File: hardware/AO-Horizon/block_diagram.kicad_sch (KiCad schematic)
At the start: 0 parts

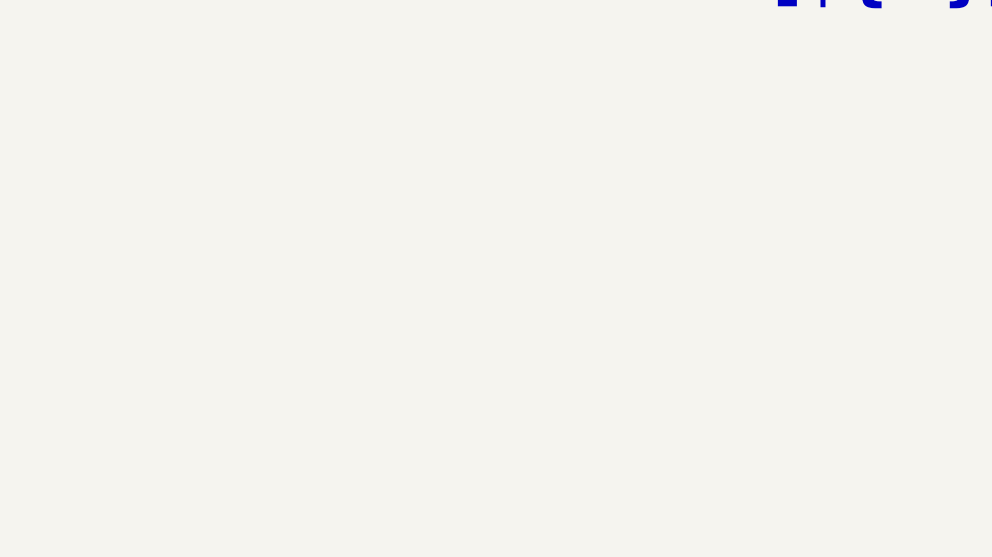
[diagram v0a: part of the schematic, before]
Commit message: feat(power): add TPS62142 3V3 buck and new library parts (#6)
* docs(readme): simplify workflow diagram explanation

Mark DRAFT as under review, sync CHECK label, and add a colour key in README and template.

Co-Authored-By: Claude Sonnet 5.5 <noreply@anthropic.com>

* Update settings.json

* change spec file name

* update git-workflow skill

* change skill name by add hw-*

* docs: update AeroOptix-Horizon hardware spec

* docs: consolidate hardware handoff into checklist

* Update CLAUDE.md

* Update CLAUDE.md

* Update CLAUDE.md

* feat(hooks): replace protect hook with rule-based v2

Move file-protection rules into hooks/protect.json (allow > deny > ask)
and use ask for editable-with-approval files instead of a hard block.
Bash/PowerShell checks now inspect write targets, not any mention of a
protected path. Align settings.json permissions and drop the old hook.

Co-Authored-By: Claude Sonnet 5.5 <noreply@anthropic.com>

* docs: update CLAUDE.md for protection tiers and skill names

Describe the ask/deny protection rules, the v2 hook and protect.json,
and fix stale skill and template names.

Co-Authored-By: Claude Sonnet 5.5 <noreply@anthropic.com>

* Update .gitignore

* Update .gitignore

* Update .gitignore

* del skills

* Update engineering.md

* Update git-workflow.md

* Update hardware-workflow.md

* Update settings.json

* Update pull_request_template.md

* Update .gitignore

* Update .gitignore

* Delete SKILL.md

* Delete SKILL.md

* Update .gitignore

* add git-workflow skill

* Update CLAUDE.md

* Update protect.json

* Update settings.json

* Create MEMORY.md

* feat(agents): add codex-hw-delegate for bounded Codex tasks

Add a project agent that delegates one small, read-only-by-default task
to Codex CLI. It gates trivial or ambiguous requests, refuses PDF and
KiCad file contents, never mutates git, cross-checks Codex output and
returns a fixed report format.

Co-Authored-By: Claude Sonnet 5.5 <noreply@anthropic.com>

* fix(hooks): resolve .. and 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
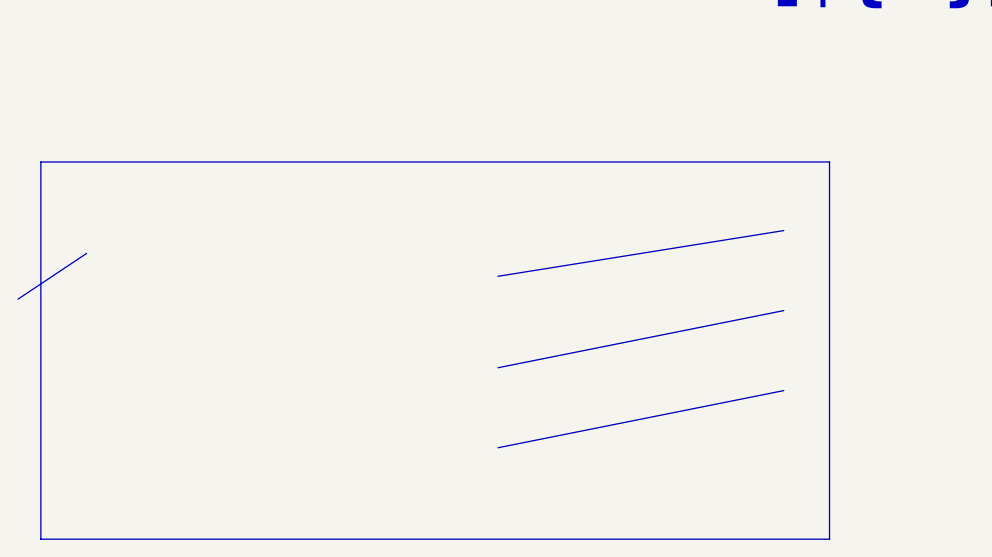
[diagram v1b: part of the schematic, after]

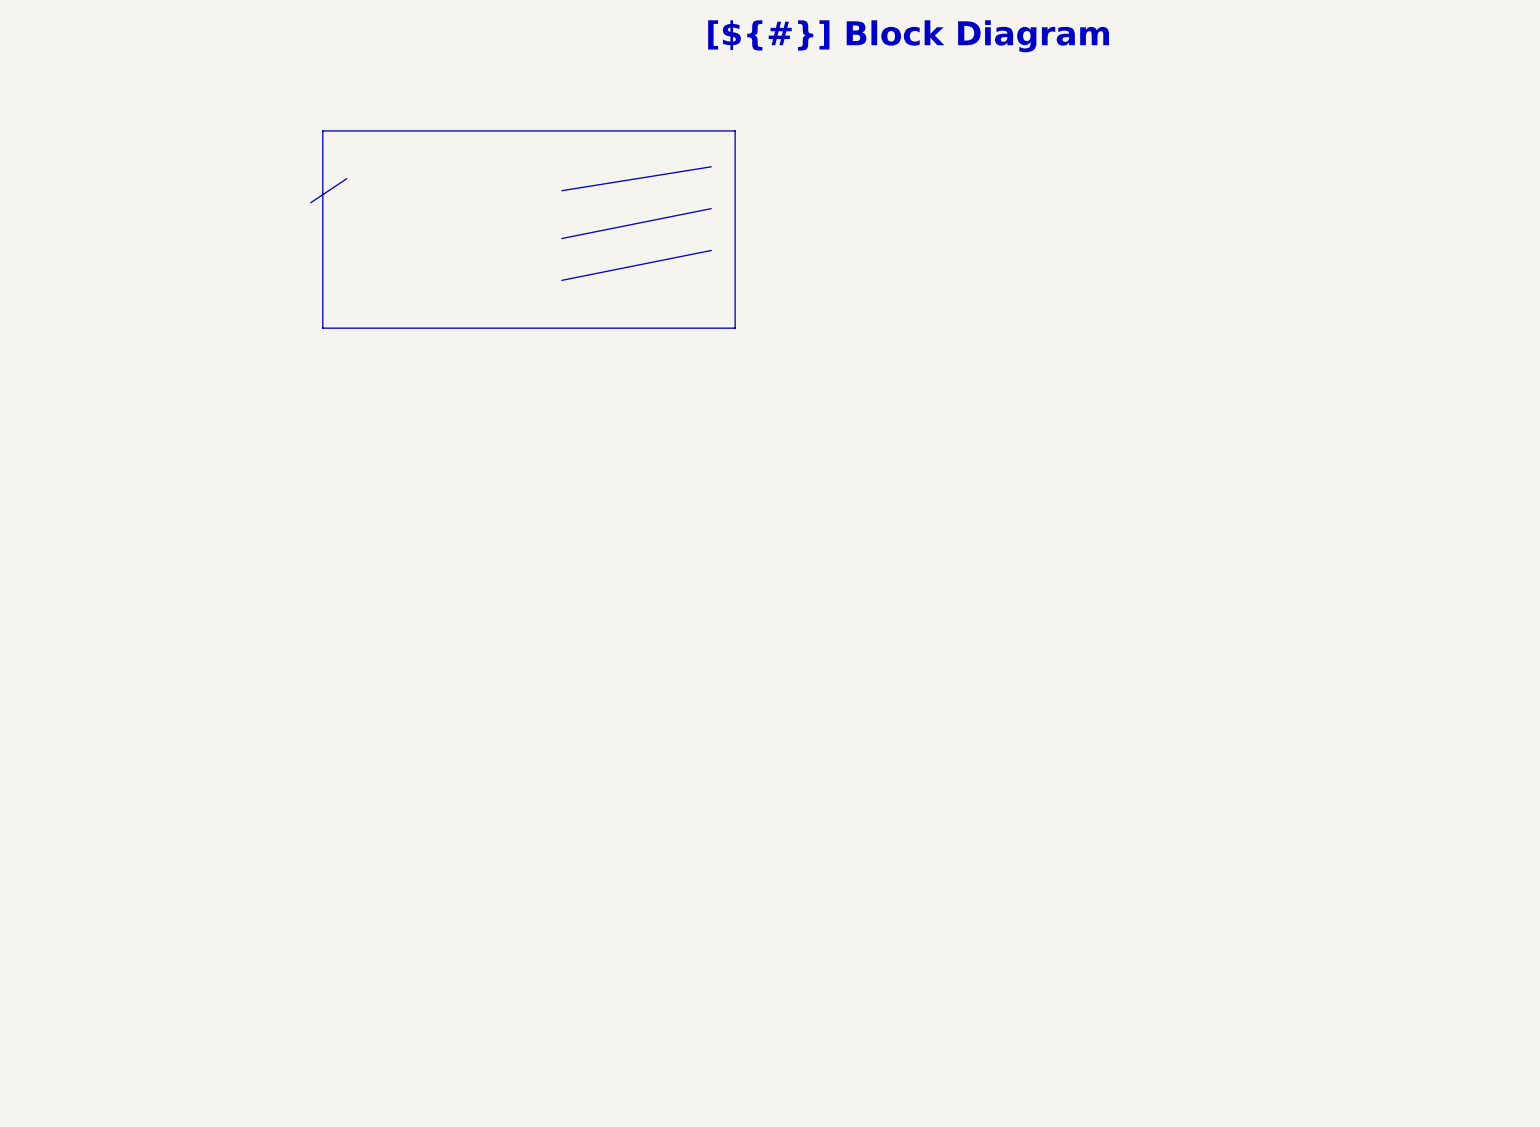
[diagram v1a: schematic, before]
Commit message: feat(library): add TPS16412 eFuse and restyle library to KLC (#11)
* docs(readme): simplify workflow diagram explanation

Mark DRAFT as under review, sync CHECK label, and add a colour key in README and template.

Co-Authored-By: Claude Sonnet 5.5 <noreply@anthropic.com>

* Update settings.json

* change spec file name

* update git-workflow skill

* change skill name by add hw-*

* docs: update AeroOptix-Horizon hardware spec

* docs: consolidate hardware handoff into checklist

* Update CLAUDE.md

* Update CLAUDE.md

* Update CLAUDE.md

* feat(hooks): replace protect hook with rule-based v2

Move file-protection rules into hooks/protect.json (allow > deny > ask)
and use ask for editable-with-approval files instead of a hard block.
Bash/PowerShell checks now inspect write targets, not any mention of a
protected path. Align settings.json permissions and drop the old hook.

Co-Authored-By: Claude Sonnet 5.5 <noreply@anthropic.com>

* docs: update CLAUDE.md for protection tiers and skill names

Describe the ask/deny protection rules, the v2 hook and protect.json,
and fix stale skill and template names.

Co-Authored-By: Claude Sonnet 5.5 <noreply@anthropic.com>

* Update .gitignore

* Update .gitignore

* Update .gitignore

* del skills

* Update engineering.md

* Update git-workflow.md

* Update hardware-workflow.md

* Update settings.json

* Update pull_request_template.md

* Update .gitignore

* Update .gitignore

* Delete SKILL.md

* Delete SKILL.md

* Update .gitignore

* add git-workflow skill

* Update CLAUDE.md

* Update protect.json

* Update settings.json

* Create MEMORY.md

* feat(agents): add codex-hw-delegate for bounded Codex tasks

Add a project agent that delegates one small, read-only-by-default task
to Codex CLI. It gates trivial or ambiguous requests, refuses PDF and
KiCad file contents, never mutates git, cross-checks Codex output and
returns a fixed report format.

Co-Authored-By: Claude Sonnet 5.5 <noreply@anthropic.com>

* fix(hooks): resolve ..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
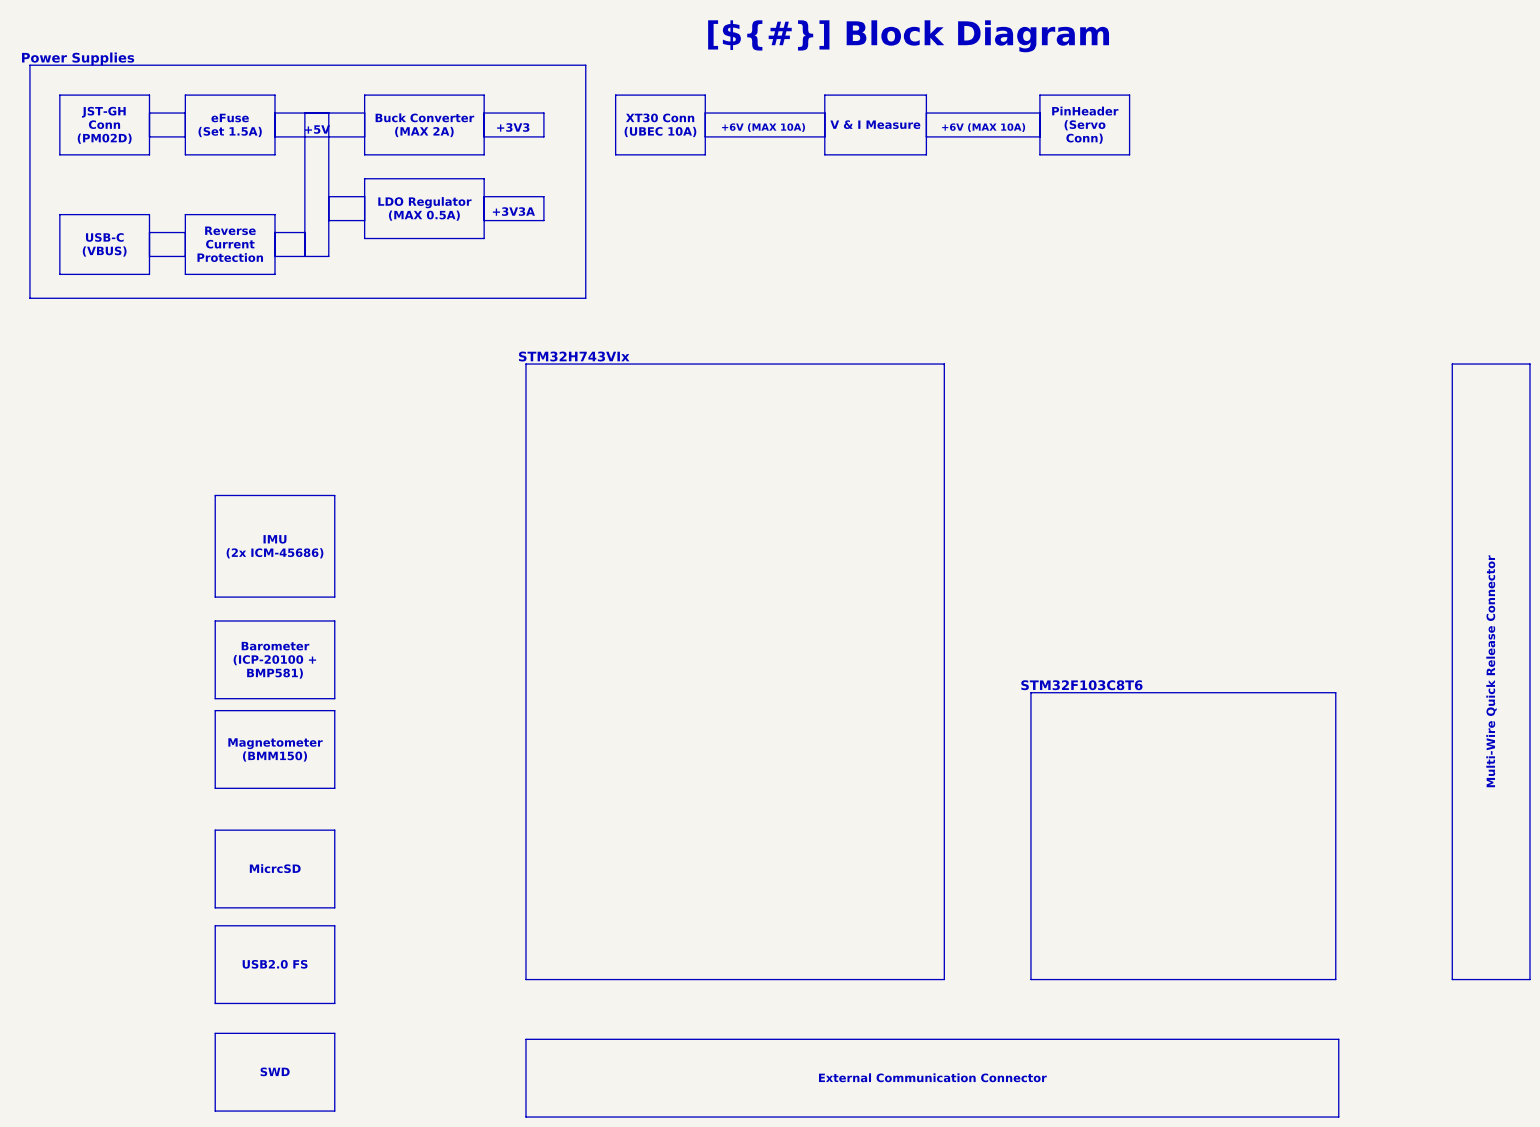
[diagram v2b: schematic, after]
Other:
- note added: "+3V3"
- note added: "+3V3A"
- note added: "+5V"
- note added: "+6V (MAX 10A)"
- note added: "Power Supplies"
- note added: "STM32F103C8T6"
- note added: "STM32H743VIx"

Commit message: feat(schematic): power sheet with wired eFuse, cleared block diagram, report PDF (#29)
* docs(readme): simplify workflow diagram explanation

Mark DRAFT as under review, sync CHECK label, and add a colour key in README and template.

Co-Authored-By: Claude Sonnet 5.5 <noreply@anthropic.com>

* Update settings.json

* change spec file name

* update git-workflow skill

* change skill name by add hw-*

* docs: update AeroOptix-Horizon hardware spec

* docs: consolidate hardware handoff into checklist

* Update CLAUDE.md

* Update CLAUDE.md

* Update CLAUDE.md

* feat(hooks): replace protect hook with rule-based v2

Move file-protection rules into hooks/protect.json (allow > deny > ask)
and use ask for editable-with-approval files instead of a hard block.
Bash/PowerShell checks now inspect write targets, not any mention of a
protected path. Align settings.json permissions and drop the old hook.

Co-Authored-By: Claude Sonnet 5.5 <noreply@anthropic.com>

* docs: update CLAUDE.md for protection tiers and skill names

Describe the ask/deny protection rules, the v2 hook and protect.json,
and fix stale skill and template names.

Co-Authored-By: Claude Sonnet 5.5 <noreply@anthropic.com>

* Update .gitignore

* Update .gitignore

* Update .gitignore

* del skills

* Update engineering.md

* Update git-workflow.md

* Update hardware-workflow.md

* Update settings.json

* Update pull_request_template.md

* Update .gitignore

* Update .gitignore

* Delete SKILL.md

* Delete SKILL.md

* Update .gitignore

* add git-workflow skill

* Update CLAUDE.md

* Update protect.json

* Update settings.json

* Create MEMORY.md

* feat(agents): add codex-hw-delegate for bounded Codex tasks

Add a project agent that delegates one small, read-only-by-default task
to Codex CLI. It gates trivial or ambiguous requests, refuses PDF and
KiCad file contents, never mutates git, cross-checks Codex output and
returns a fixed report format.

Co-Authored-By: Claude Sonnet 5.5 <noreply@anthropic.com>

* fi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
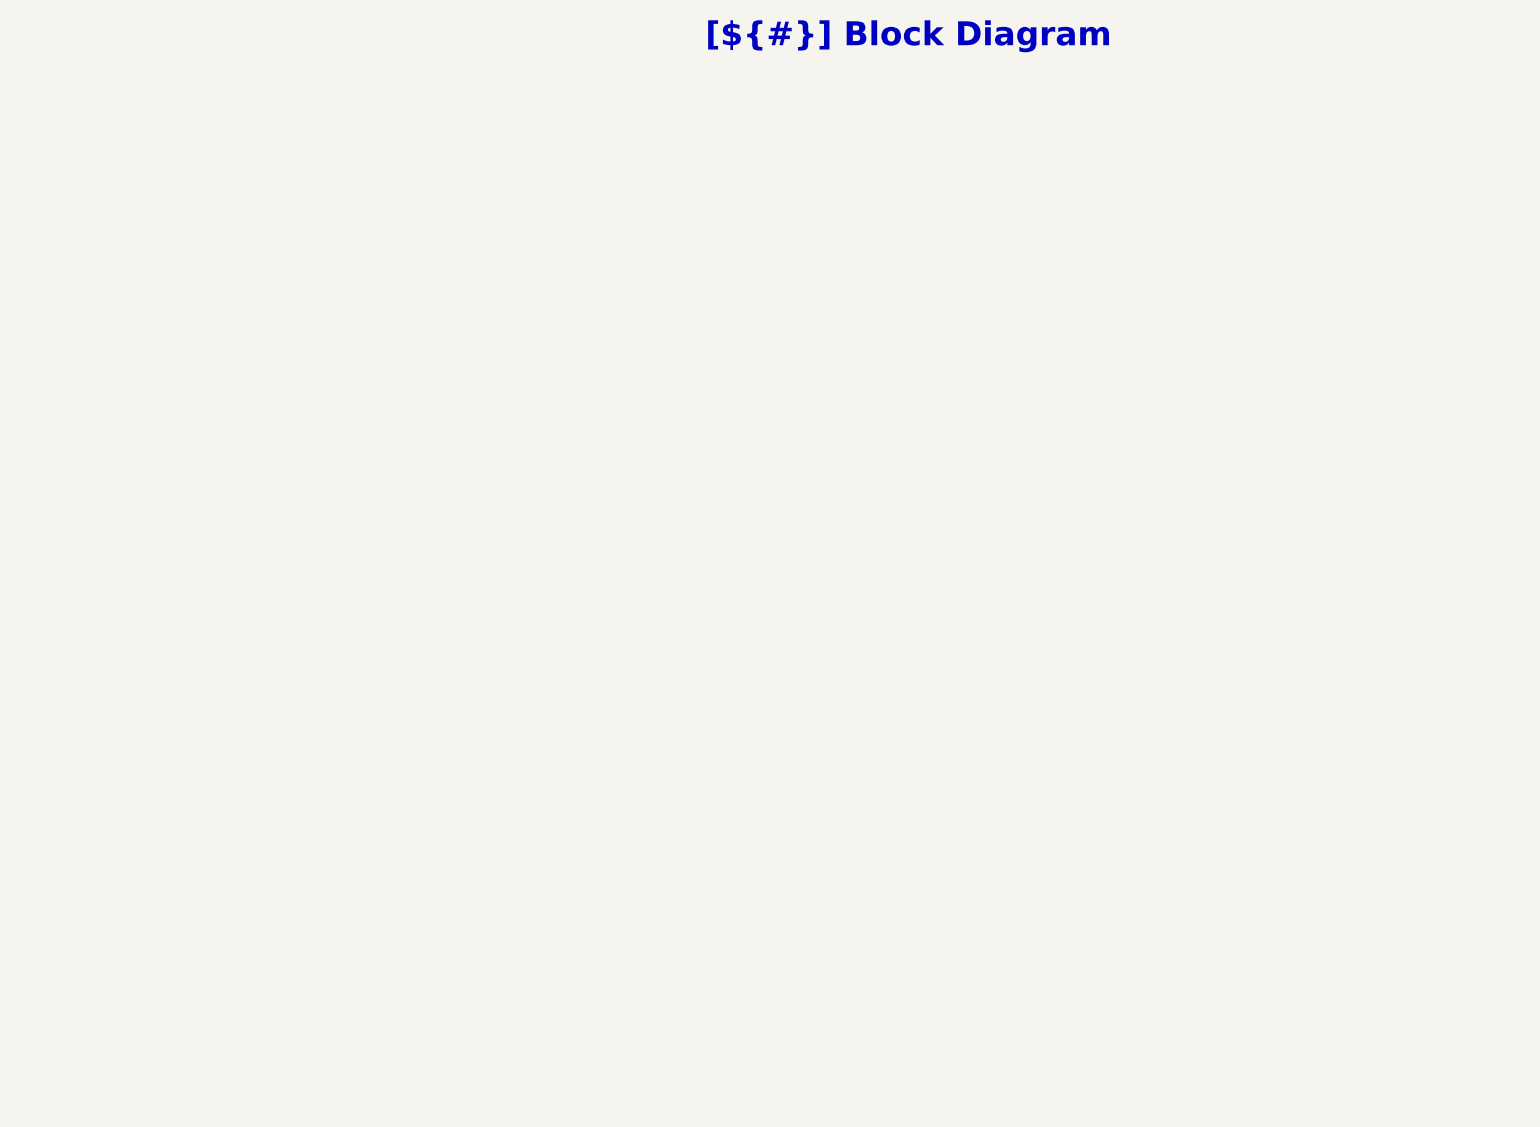
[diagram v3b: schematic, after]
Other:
- note removed: "+3V3"
- note removed: "+3V3A"
- note removed: "+5V"
- note removed: "+6V (MAX 10A)"
- note removed: "Power Supplies"
- note removed: "STM32F103C8T6"
- note removed: "STM32H743VIx"
